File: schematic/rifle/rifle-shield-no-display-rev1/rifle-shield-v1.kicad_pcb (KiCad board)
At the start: 2 copper layers, 50 x 26.2 mm, 38 parts, among them K1 CONN_3, P1 Power, P10 MCU2, P11 RFID-RC522-MODULE, P12 NRF24L01, P13 IR_LED, P15 Vibro&flash, P2 MCU1, P3 Mag&fireMode, P4 VCC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

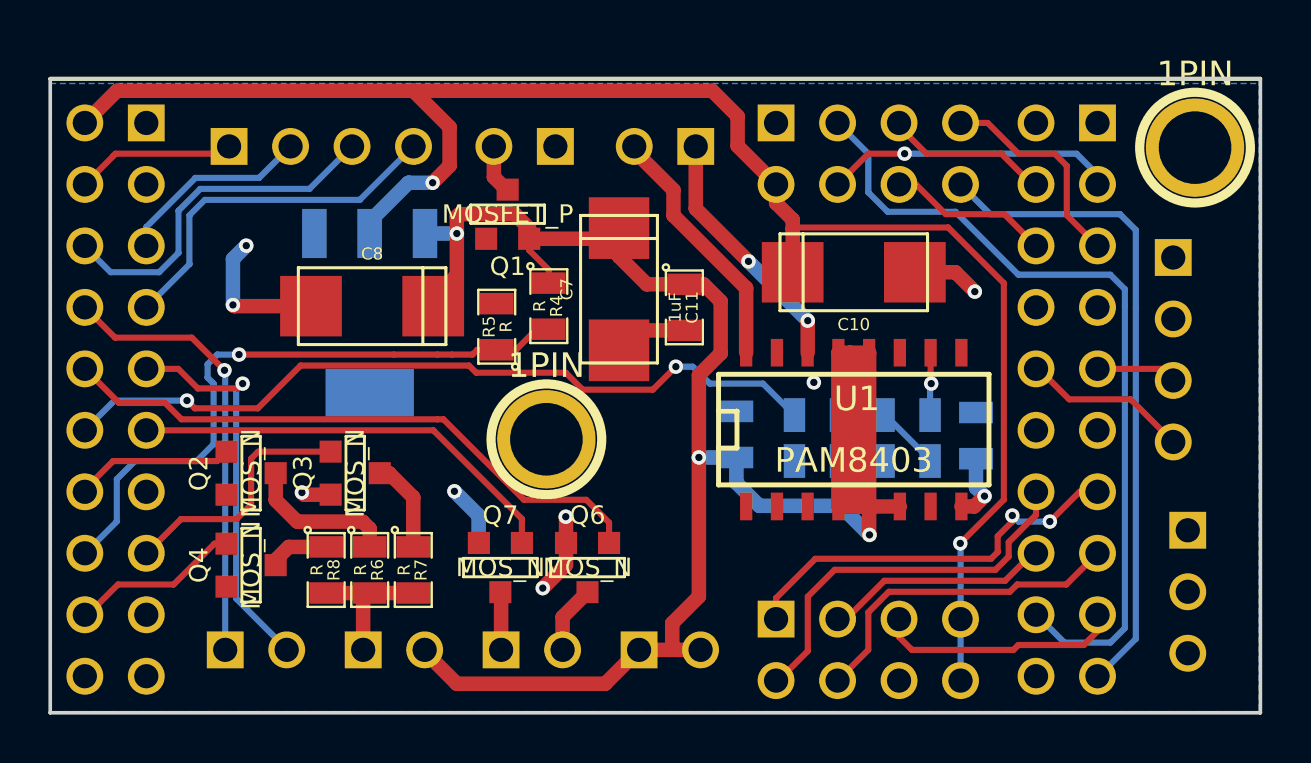
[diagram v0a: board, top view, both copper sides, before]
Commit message: PCB: MCU2 connector orientation fixed; SOFT: Worker object added to os-wrappers, WavPlayer and IOPinsPool use it now
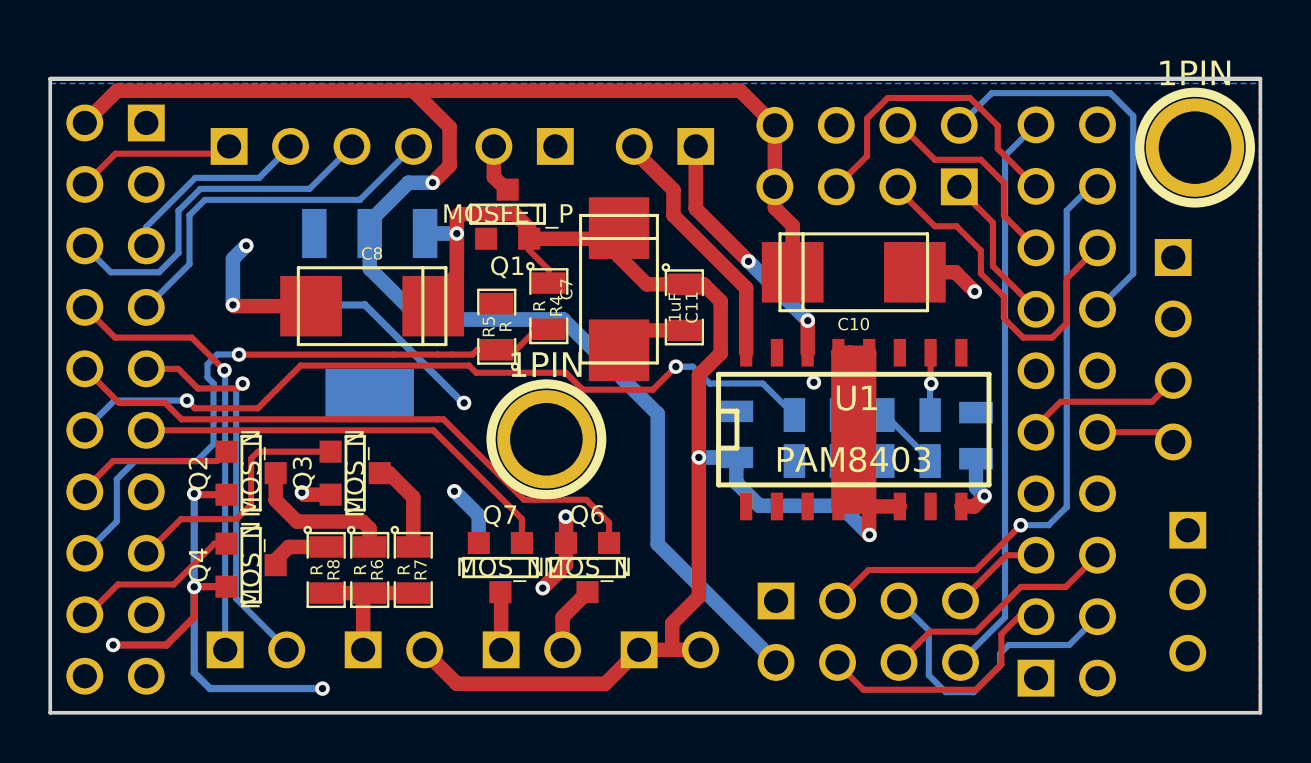
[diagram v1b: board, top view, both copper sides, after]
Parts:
- moved P11 20.4 mm to (96.5, 49.0), turned to 180 degrees
- moved P12 19.8 mm to (96.6, 68.7)
- turned P10 to 90 degrees
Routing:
- net GND: track 18.9 -> 48.3 mm, vias 7 -> 11
- net N-0000016: track 16.7 -> 6.37 mm, vias 2 -> 0
- net N-0000021: track 34.0 -> 25.0 mm, vias 0 -> 1
- net N-0000023: track 6.79 -> 12.4 mm
- net N-0000018: track 9.33 -> 14.6 mm
- net N-0000020: track 13.8 -> 8.60 mm
- net N-0000025: track 8.96 -> 3.90 mm
- net N-000002: track 27.1 -> 23.5 mm
- net N-0000031: track 6.92 -> 3.30 mm
- net N-0000032: track 3.33 -> 6.70 mm
- net N-0000024: track 6.71 -> 10.0 mm
- net N-0000015: track 10.2 -> 12.7 mm
- net (no net): track 0.00 -> 2.56 mm, vias 1 -> 2
- net +3.3V: track 70.9 -> 72.6 mm, vias 2 -> 1
- net N-0000022: track 12.0 -> 10.7 mm, vias 1 -> 0
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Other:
- net class Default: trace_width 0.6 -> 0.3
- board text added: "Caustic LT system rifle shield v1 nd rev.2"
- board text removed: "Caustic LT system rifle shield v1 ND rev.1"

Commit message: Fix for heartbeat; IDC sensor; rifle shield in process
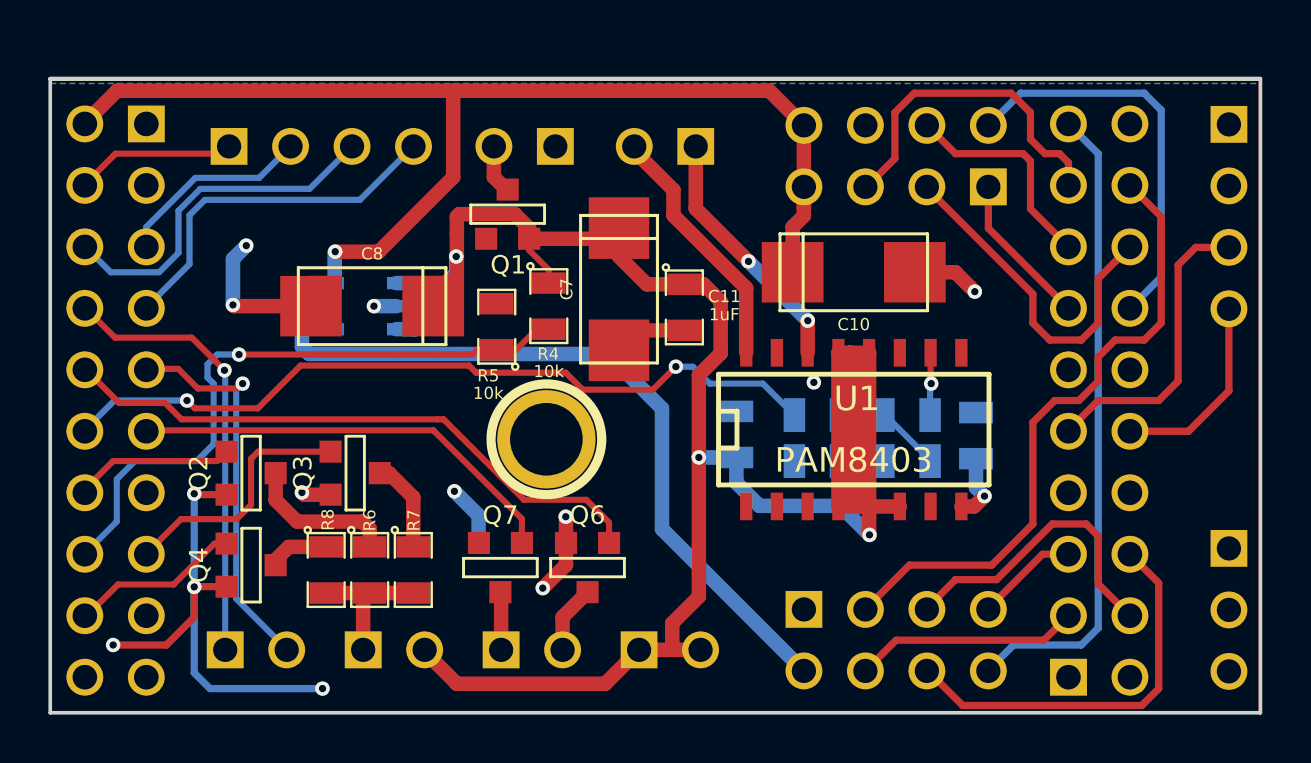
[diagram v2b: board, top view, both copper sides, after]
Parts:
- removed 1PIN: P***, 1pin
- C3: value C -> 0.015uF
- Q1: value MOSFET_P -> (none)
- Q2, Q3, Q4: value MOS_N -> (none)
- R1, R3, R4, R5: value R -> 10k
- R6, R7, R8: value R -> (none)
- U2: value LINSTAB-(1-GND/ADJ,2-OUT,3-IN) -> NCP551; footprint SOT223 -> SOT23-5
- moved P6 5.96 mm to (111.5, 51.5)
- moved K1 1.86 mm to (111.5, 67.8)
- moved P10 1.34 mm to (106.1, 59.1)
- moved P12 1.20 mm to (97.8, 69.0)
- moved P11 1.20 mm to (97.8, 49.0)
- moved U2 0.35 mm to (75.8, 55.2), turned to 270 degrees
- renumbered 1PIN to ?
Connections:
- U2 pad 1: GND -> VCC
- U2 pad 2: +3.3V -> GND
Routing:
- net GND: track 48.3 -> 38.0 mm
- net +3.3V: track 72.6 -> 82.0 mm
- net N-0000016: track 10.0 -> 16.5 mm
- net N-0000029: track 6.70 -> 12.6 mm
- net VCC: track 88.7 -> 93.6 mm
- net N-0000028: track 3.30 -> 8.17 mm
- net N-0000023: track 23.5 -> 26.6 mm
- net N-0000025: track 25.0 -> 26.4 mm, vias 1 -> 0
- net N-0000026: track 10.7 -> 9.33 mm
- net N-0000019: track 12.7 -> 13.9 mm
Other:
- net class Default: trace_width 0.3 -> 0.6

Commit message: rifle shield sended
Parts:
- renumbered P11 to RFID, P13 to e, P12 to nrf24l01
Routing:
- net (no net): vias 2 -> 1
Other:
- board text added: "Caustic LT system rifle shield no displ. rev.3"
- board text removed: "Caustic LT system rifle shield v1 nd rev.2"
- board text removed: "MCU1"
- board text removed: "MCU2"
- board text removed: "RFID"
- board text removed: "nfr24l01"
